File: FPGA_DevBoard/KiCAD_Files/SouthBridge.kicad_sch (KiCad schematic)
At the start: 30 parts, among them IC2 TAD5242IRGER, J9 SJ3-35083A-TR, U15 ESP32-WROOM-32UE-N8

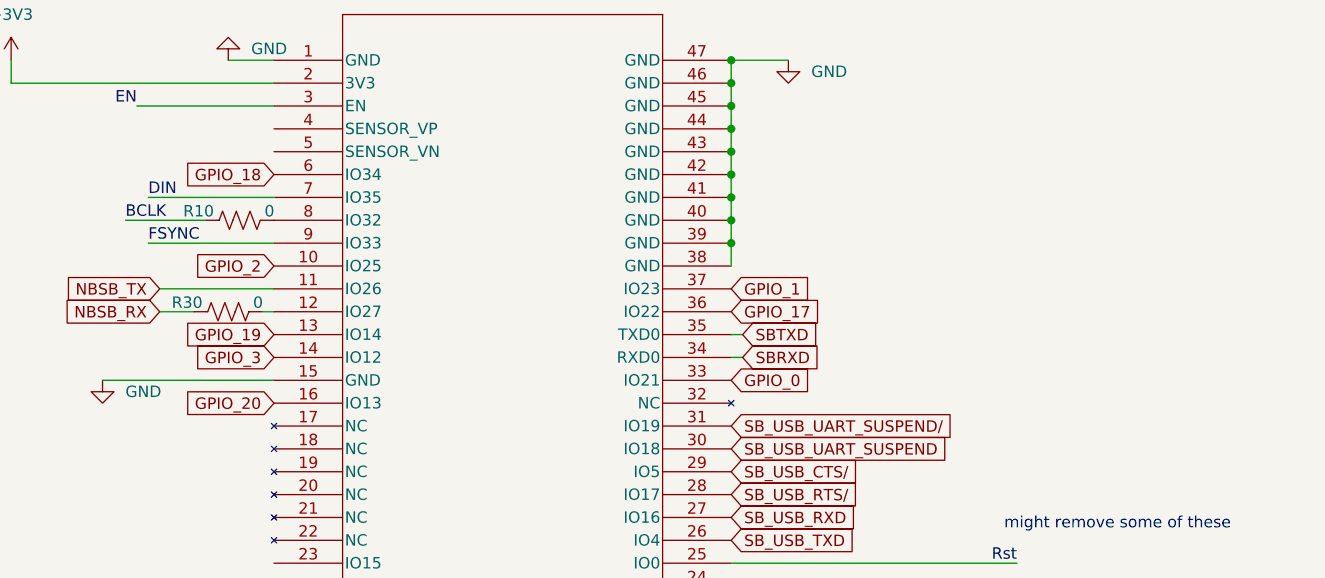
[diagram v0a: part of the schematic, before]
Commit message: ESD
Added ESD to the main USB programmer. Also added terminating resistors and test points. Also updated some planes to make sure everything was connected.
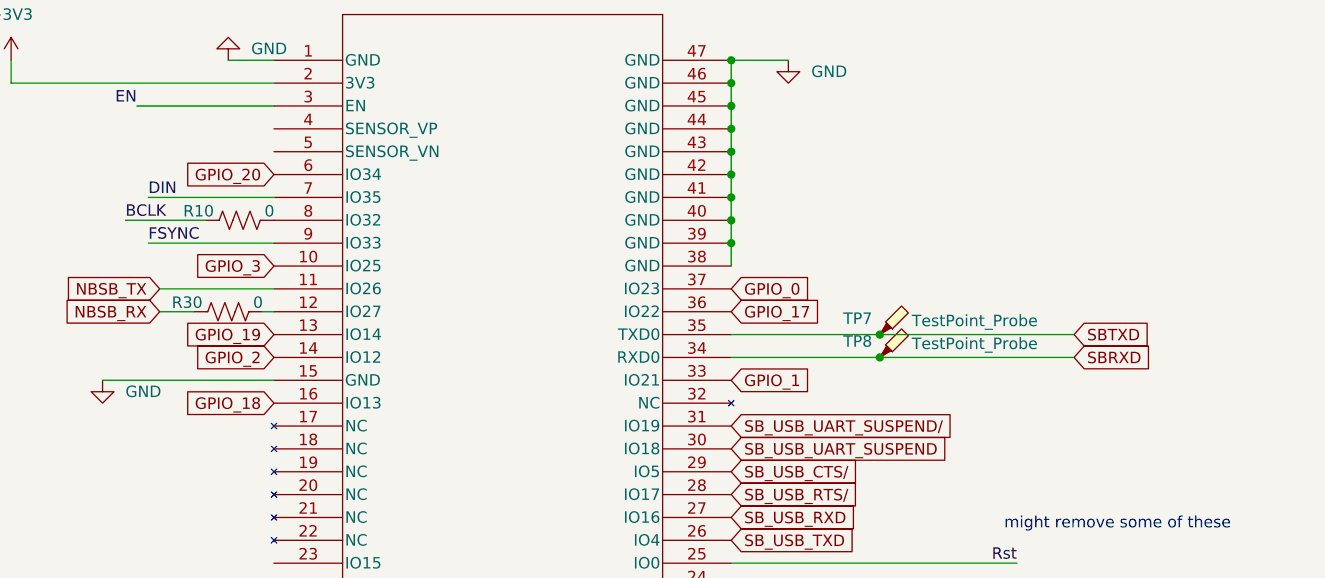
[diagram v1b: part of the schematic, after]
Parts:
- added TP7, TP8: TestPoint_Probe, TestPoint:TestPoint_Pad_D1.0mm, symbol Connector:TestPoint_Probe
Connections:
- net GPIO_0: now also U15.37 (IO23); no longer U15.33 (IO21)
- net GPIO_1: now also U15.33 (IO21); no longer U15.37 (IO23)
- net GPIO_18: now also U15.16 (IO13); no longer U15.6 (IO34)
- net GPIO_2: now also U15.14 (IO12); no longer U15.10 (IO25)
- net GPIO_20: now also U15.6 (IO34); no longer U15.16 (IO13)
- net GPIO_3: now also U15.10 (IO25); no longer U15.14 (IO12)
- net SBRXD: now also TP8.1
- net SBTXD: now also TP7.1
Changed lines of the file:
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@@
+	)
+	(junction
+		(at 118.11 82.55)
+		(diameter 0)
+		(color 0 0 0 0)
 	)
 	(junction
@@
 	)
 	(junction
+		(at 118.11 80.01)
+		(diameter 0)
+		(color 0 0 0 0)
+	)
+	(junction
 		(at 257.81 100.33)
 		(diameter 0)
@@
 	(wire
 		(pts
+			(xy 118.11 82.55) (xy 139.7 82.55)
+		)
+		(stroke
+			(width 0)
+			(type default)
+		)
+	)
+	(wire
+		(pts
 			(xy 274.32 76.2) (xy 266.7 76.2)
 		)
@@
 	(wire
 		(pts
-			(xy 101.6 80.01) (xy 102.87 80.01)
+			(xy 101.6 80.01) (xy 118.11 80.01)
 		)
 		(stroke
@@
 	(wire
 		(pts
-			(xy 101.6 82.55) (xy 102.87 82.55)
+			(xy 101.6 82.55) (xy 118.11 82.55)
 		)
 		(stroke
@@
 		(pts
 			(xy 266.7 100.33) (xy 275.59 100.33)
+		)
+		(stroke
+			(width 0)
+			(type default)
+		)
+	)
+	(wire
+		(pts
+			(xy 118.11 80.01) (xy 139.7 80.01)
 		)
 		(stroke
@@
 		)
 	)
-	(global_label "GPIO_0"
+	(global_label "GPIO_2"
 		(shape input)
-		(at 101.6 85.09 0)
+		(at 50.8 82.55 180)
 		(fields_autoplaced yes)
 		(effects
@@
 				(size 1.27 1.27)
 			)
-			(justify left)
+			(justify right)
 		)
 		(property "Intersheetrefs" "${INTERSHEET_REFS}"
-			(at 111.2376 85.09 0)
-			(effects
-				(font
-					(size 1.27 1.27)
-				)
-				(justify left)
+			(at 41.1624 82.55 0)
+			(effects
+				(font
+					(size 1.27 1.27)
+				)
+				(justify right)
+				(hide yes)
+			)
+		)
+	)
+	(global_label "GPIO_18"
+		(shape input)
+		(at 50.8 87.63 180)
+		(fields_autoplaced yes)
+		(effects
+			(font
+				(size 1.27 1.27)
+			)
+			(justify right)
+		)
+		(property "Intersheetrefs" "${INTERSHEET_REFS}"
+			(at 39.9529 87.63 0)
+			(effects
+				(font
+					(size 1.27 1.27)
+				)
+				(justify right)
 				(hide yes)
 			)
@@
 		)
 	)
-	(global_label "GPIO_1"
-		(shape input)
-		(at 101.6 74.93 0)
-		(fields_autoplaced yes)
-		(effects
-			(font
-				(size 1.27 1.27)
-			)
-			(justify left)
-		)
-		(property "Intersheetrefs" "${INTERSHEET_REFS}"
-			(at 111.2376 74.93 0)
-			(effects
-				(font
-					(size 1.27 1.27)
-				)
-				(justify left)
-				(hide yes)
-			)
-		)
-	)
-	(global_label "GPIO_18"
+	(global_label "GPIO_20"
 		(shape input)
 		(at 50.8 62.23 180)
@@
 		)
 	)
-	(global_label "GPIO_3"
-		(shape input)
-		(at 50.8 82.55 180)
-		(fields_autoplaced yes)
-		(effects
-			(font
-				(size 1.27 1.27)
-			)
-			(justify right)
-		)
-		(property "Intersheetrefs" "${INTERSHEET_REFS}"
-			(at 41.1624 82.55 0)
-			(effects
-				(font
-					(size 1.27 1.27)
-				)
-				(justify right)
-				(hide yes)
-			)
-		)
-	)
-	(global_label "GPIO_20"
-		(shape input)
-		(at 50.8 87.63 180)
-		(fields_autoplaced yes)
-		(effects
-			(font
-				(size 1.27 1.27)
-			)
-			(justify right)
-		)
-		(property "Intersheetrefs" "${INTERSHEET_REFS}"
-			(at 39.9529 87.63 0)
-			(effects
-				(font
-					(size 1.27 1.27)
-				)
-				(justify right)
-				(hide yes)
-			)
-		)
-	)
 	(global_label "SBTXD"
 		(shape input)
-		(at 102.87 80.01 0)
+		(at 139.7 80.01 0)
 		(fields_autoplaced yes)
 		(effects
@@
 		)
 		(property "Intersheetrefs" "${INTERSHEET_REFS}"
-			(at 111.7818 80.01 0)
+			(at 148.6118 80.01 0)
 			(effects
 				(font
@@
 		)
 	)
-	(global_label "GPIO_2"
+	(global_label "GPIO_1"
+		(shape input)
+		(at 101.6 85.09 0)
+		(fields_autoplaced yes)
+		(effects
+			(font
+				(size 1.27 1.27)
+			)
+			(justify left)
+		)
+		(property "Intersheetrefs" "${INTERSHEET_REFS}"
+			(at 111.2376 85.09 0)
+			(effects
+				(font
+					(size 1.27 1.27)
+				)
+				(justify left)
+				(hide yes)
+			)
+		)
+	)
+	(global_label "GPIO_3"
 		(shape input)
 		(at 50.8 72.39 180)
@@
 		)
 	)
+	(global_label "GPIO_0"
+		(shape input)
+		(at 101.6 74.93 0)
+		(fields_autoplaced yes)
+		(effects
+			(font
+				(size 1.27 1.27)
+			)
+			(justify left)
+		)
+		(property "Intersheetrefs" "${INTERSHEET_REFS}"
+			(at 111.2376 74.93 0)
+			(effects
+				(font
+					(size 1.27 1.27)
+				)
+				(justify left)
+				(hide yes)
+			)
+		)
+	)
 	(global_label "SB_USB_UART_SUSPEND{slash}"
 		(shape input)
@@
 	(global_label "SBRXD"
 		(shape input)
-		(at 102.87 82.55 0)
+		(at 139.7 82.55 0)
 		(fields_autoplaced yes)
 		(effects
@@
 		)
 		(property "Intersheetrefs" "${INTERSHEET_REFS}"
-			(at 112.0842 82.55 0)
+			(at 148.9142 82.55 0)
 			(effects
 				(font
@@
 				(justify left)
 				(hide yes)
+			)
+		)
+	)
+	(symbol
+		(lib_id "Connector:TestPoint_Probe")
+		(at 118.11 80.01 0)
+		(unit 1)
+		(exclude_from_sim no)
+		(in_bom yes)
+		(on_board yes)
+		(dnp no)
+		(property "Reference" "TP7"
+			(at 114.046 78.232 0)
+			(effects
+				(font
+					(size 1.27 1.27)
+				)
+				(justify left)
+			)
+		)
+		(property "Value" "TestPoint_Probe"
+			(at 121.666 78.486 0)
+			(effects
+				(font
+					(size 1.27 1.27)
+				)
+				(justify left)
+			)
+		)
+		(property "Footprint" "TestPoint:TestPoint_Pad_D1.0mm"
+			(at 123.19 80.01 0)
+			(effects
+				(font
+					(size 1.27 1.27)
+				)
+				(hide yes)
+			)
+		)
+		(property "Datasheet" "~"
+			(at 123.19 80.01 0)
+			(effects
+				(font
+					(size 1.27 1.27)
+				)
+				(hide yes)
+			)
+		)
+		(property "Description" "test point (alternative probe-style design)"
+			(at 118.11 80.01 0)
+			(effects
+				(font
+					(size 1.27 1.27)
+				)
+				(hide yes)
+			)
+		)
+		(pin "1"
+		)
+		(instances
+			(project "FPGA_DevBoard"
+				(path "/29dacc10-fb0d-42da-8b4b-fe903faf3f1a/fe3059ee-eacc-43e0-b8fb-e8333ff871ae"
+					(reference "TP7")
+					(unit 1)
+				)
 			)
 		)
@@
 					(unit 1)
 				)
+			)
+		)
+	)
+	(symbol
+		(lib_id "Connector:TestPoint_Probe")
+		(at 118.11 82.55 0)
+		(unit 1)
+		(exclude_from_sim no)
+		(in_bom yes)
+		(on_board yes)
+		(dnp no)
+		(property "Reference" "TP8"
+			(at 114.046 80.772 0)
+			(effects
+				(font
+					(size 1.27 1.27)
+				)
+				(justify left)
+			)
+		)
+		(property "Value" "TestPoint_Probe"
+			(at 121.666 81.026 0)
+			(effects
+				(font
+					(size 1.27 1.27)
+				)
+				(justify left)
+			)
+		)
+		(property "Footprint" "TestPoint:TestPoint_Pad_D1.0mm"
+			(at 123.19 82.55 0)
+			(effects
+				(font
+					(size 1.27 1.27)
+				)
+				(hide yes)
+			)
+		)
+		(property "Datasheet" "~"
+			(at 123.19 82.55 0)
+			(effects
+				(font
+					(size 1.27 1.27)
+				)
+				(hide yes)
+			)
+		)
+		(property "Description" "test point (alternative probe-style design)"
+			(at 118.11 82.55 0)
+			(effects
+				(font
+					(size 1.27 1.27)
+				)
+				(hide yes)
+			)
+		)
+		(pin "1"
+		)
+		(instances
+			(project "FPGA_DevBoard"
+				(path "/29dacc10-fb0d-42da-8b4b-fe903faf3f1a/fe3059ee-eacc-43e0-b8fb-e8333ff871ae"
+					(reference "TP8")
+					(unit 1)
+				)

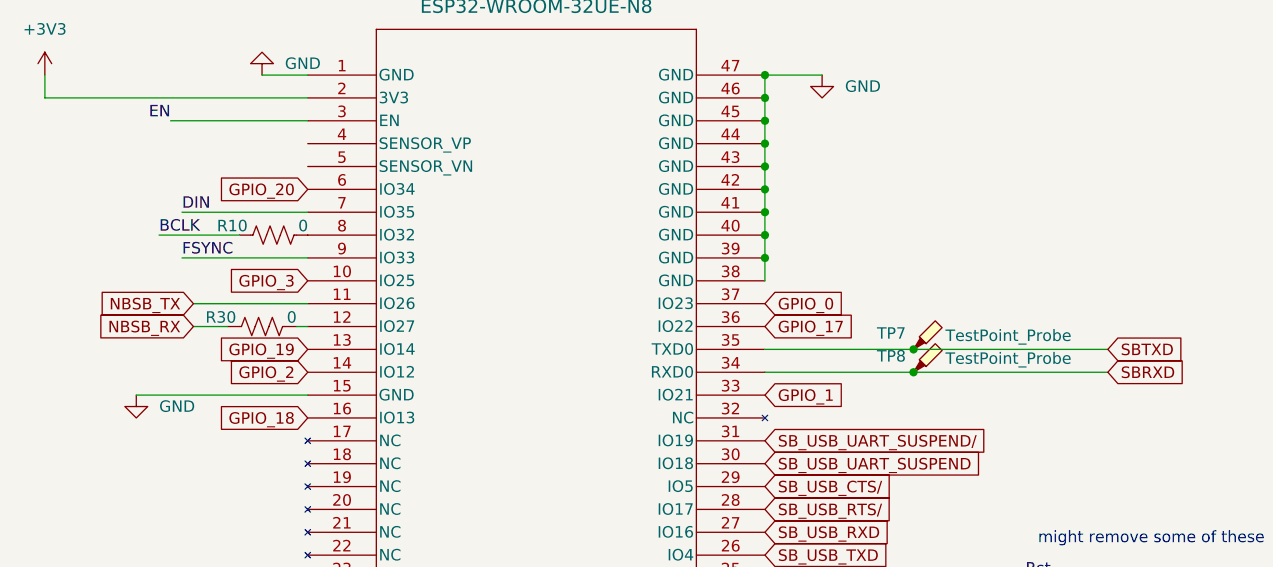
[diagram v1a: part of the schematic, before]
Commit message: Updated the NBSB IO to not go to input only, need to change this on the layout. Updated the FPGA clk to go to a positive differential signal with MCRR - need to change on layout. Updated the USB-UART bridge to not have Regin grounded - need to change on layout.
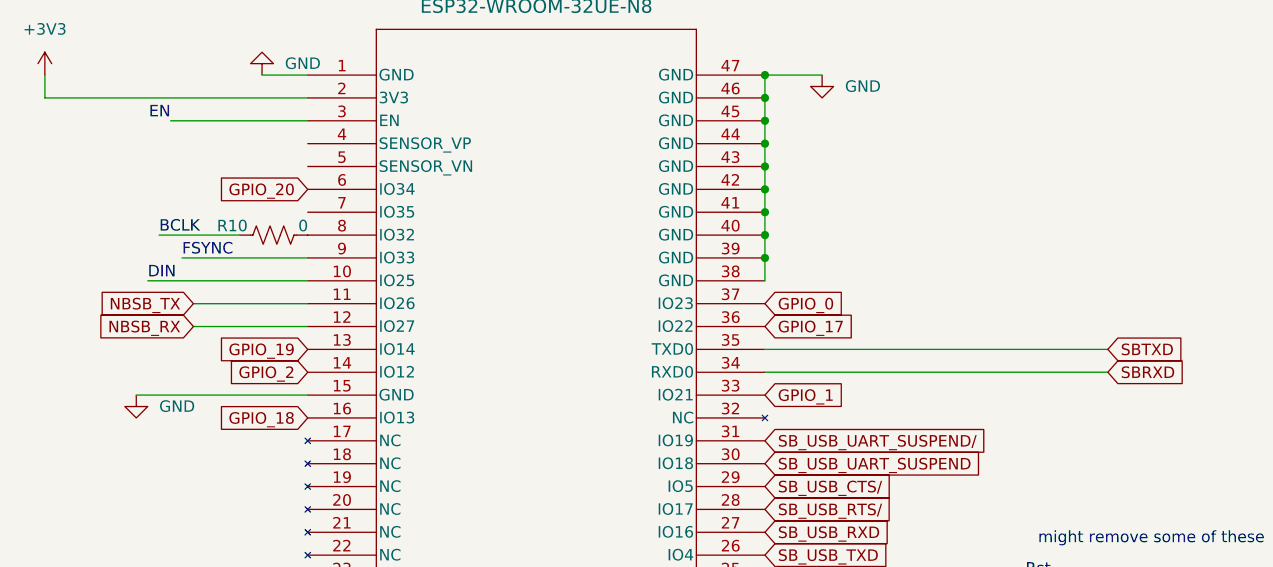
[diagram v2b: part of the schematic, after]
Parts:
- removed R30: 0, Resistor_SMD:R_0603_1608Metric, symbol Device:R_US
- removed TP7, TP8: TestPoint_Probe, TestPoint:TestPoint_Pad_D1.0mm, symbol Connector:TestPoint_Probe
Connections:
- net GPIO_3 is gone; now on net DIN: U15.10 (IO25)
- net DIN: no longer U15.7 (IO35)
- net NBSB_RX: now also U15.12 (IO27)

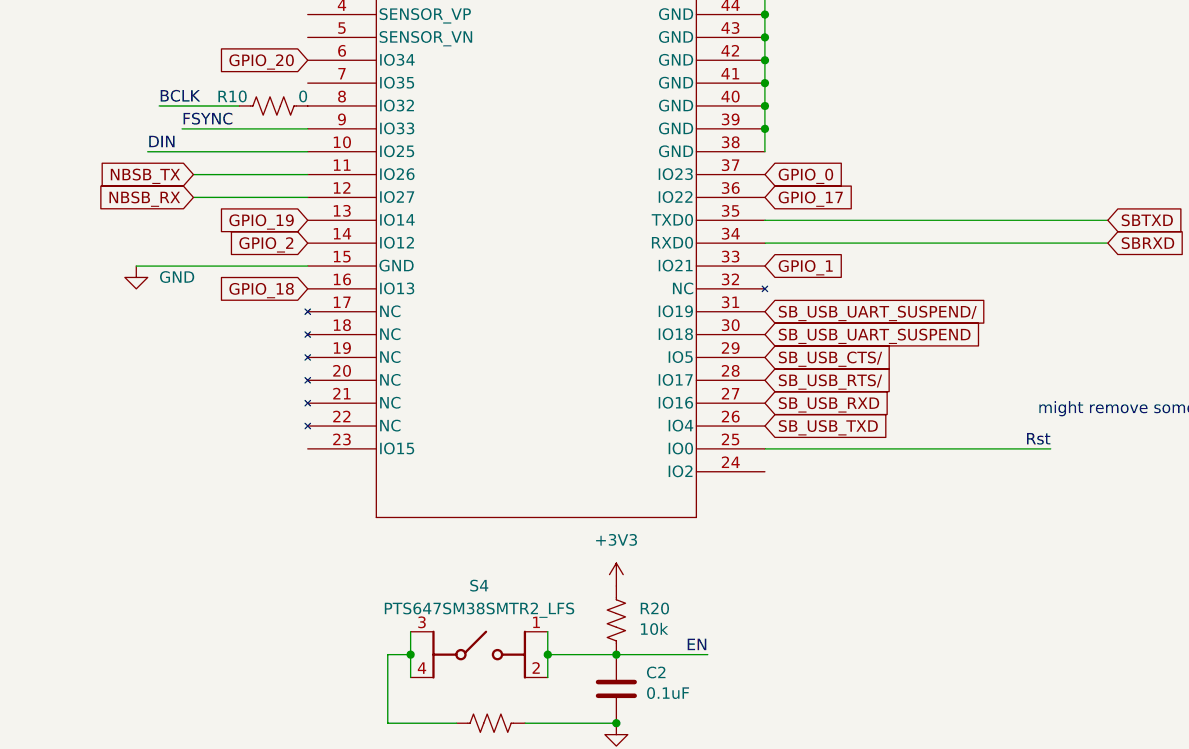
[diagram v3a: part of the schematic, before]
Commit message: Universal Serial Bussin it down
Replaced the USB Hub with the new USB Hosts, added a clock reset button, moved some things on the silk screen.
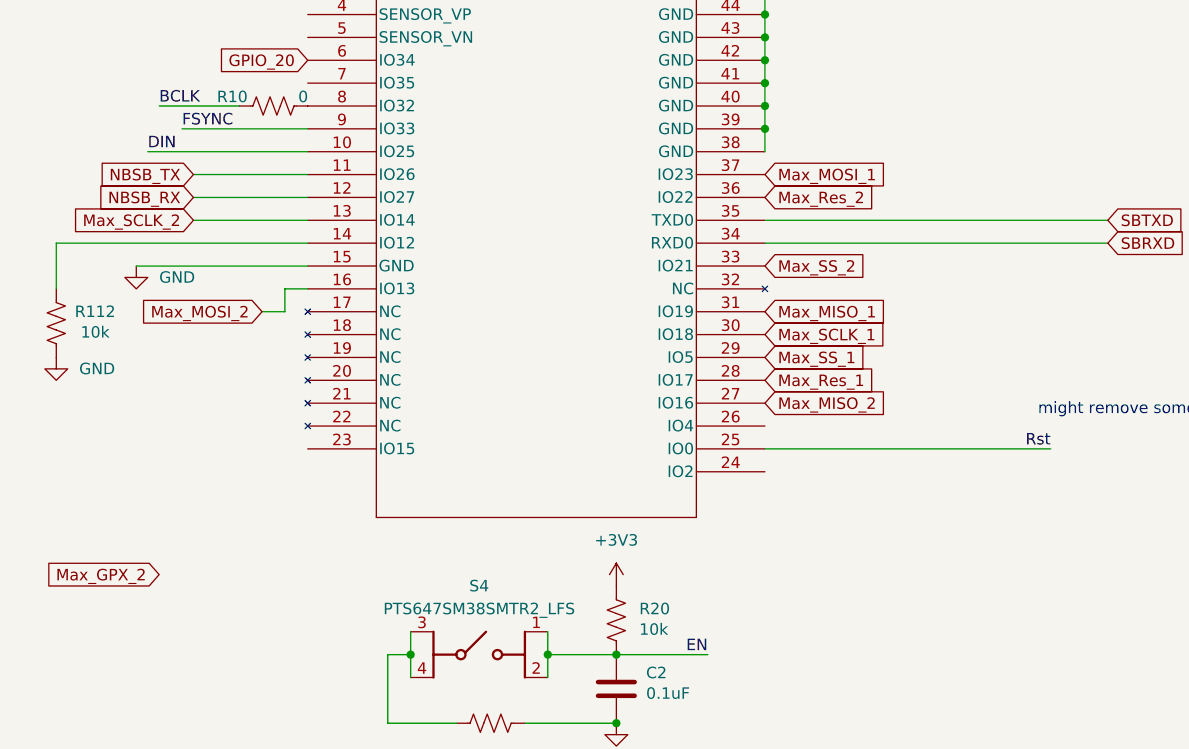
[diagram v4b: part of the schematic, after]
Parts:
- added R112: 10k, Resistor_SMD:R_0402_1005Metric, symbol Device:R_US
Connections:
- net GND: now also R112.1
- net GPIO_0 renamed Max_MOSI_1
- net GPIO_1 renamed Max_SS_2
- net GPIO_17 renamed Max_Res_2
- net GPIO_18 renamed Max_MOSI_2
- net GPIO_19 renamed Max_SCLK_2
- net GPIO_2: no longer names the net of U15.14 (IO12)
- net GPIO_2: now also R112.2
- net SB_USB_CTS/ renamed Max_SS_1
- net SB_USB_RTS/ renamed Max_Res_1
- net SB_USB_RXD renamed Max_MISO_2
- net SB_USB_TXD: no longer names the net of U15.26 (IO4)
- net SB_USB_UART_SUSPEND renamed Max_SCLK_1
- net SB_USB_UART_SUSPEND/ renamed Max_MISO_1

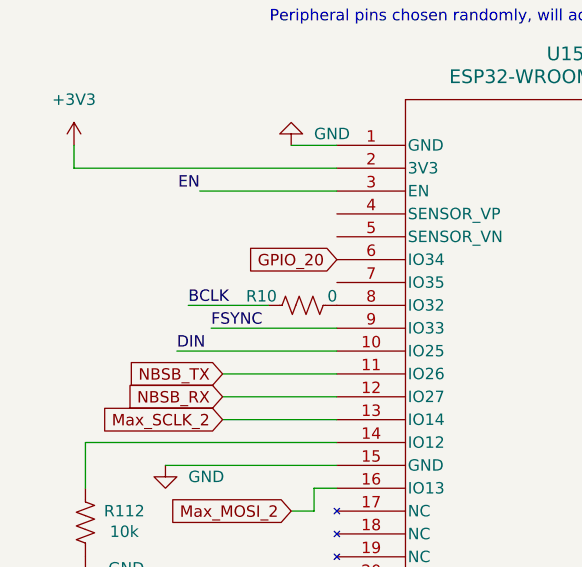
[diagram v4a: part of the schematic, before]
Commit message: VGA LENGTH MATCH, LED
Length matched the VGA, updated the GPIO to use the usb host gpio, added some leds and fixed the silkscreen more
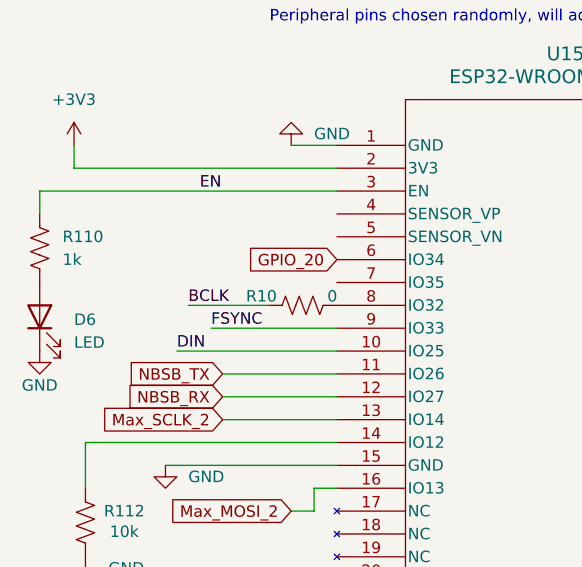
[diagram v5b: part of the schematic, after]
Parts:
- added D6: LED, Diode_SMD:D_0603_1608Metric, symbol Device:LED
- added R110: 1k, Resistor_SMD:R_0603_1608Metric, symbol Device:R_US
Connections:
- net EN: now also R110.1
- net GND: now also D6.1 (K)
- new net: D6.2 (A), R110.2

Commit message: Final Final Final Lol
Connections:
- net Max_GPX_2: now also U15.23 (IO15)
- net Max_GPX_1: now reaches U15.26 (IO4)
- net Max2_Int: now reaches U15.7 (IO35)
- net GPIO_20 renamed Max1_Int
- no-connect marks 0 -> 4
